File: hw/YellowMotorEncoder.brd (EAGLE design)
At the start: 35 x 22.2 mm, 20 parts, among them P1 M1

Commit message: FourProbes
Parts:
- removed C2: 10n/50V, rcl:C0402
- removed JP1: (no value), pinhead:1X06
- removed U$3: YELLOW_MOTOR, motor:YELLOW_MOTOR
- added C10: 20n/50V, rcl:C0402
- added C8, C9: 18p/50V, rcl:C0402
- added M1: MOTOR, motor:OT-FK-130PH
- added R6, R7: 47k, rcl:R0402
- added U$4, U$5: MH253ESO, hall_sensor:SOT23
- added U1: SN74LVC2G86DCTR, SN74LVC2G86DCTR:SOP65P400X130-8N
- C1: value 10n/50V -> 20n/50V
- R1, R2, R3, R4, R5: device rcl:R0603 -> rcl:R0402
- moved C3 29.9 mm to (2.00, 7.30)
- moved C5 23.5 mm to (8.85, 4.55), turned to 0 degrees
- moved C4 18.4 mm to (18.1, 7.40), turned to 270 degrees
- moved LED_B 17.8 mm to (18.4, 1.30), turned to 0 degrees
- moved P1 15.7 mm to (10.8, 1.90), turned to 180 degrees
- moved R3 13.6 mm to (18.4, 3.50), turned to 270 degrees
- moved LED_A 13.3 mm to (2.95, 1.30), turned to 0 degrees
- moved R2 13.3 mm to (2.95, 3.60), turned to 270 degrees
- moved LED_POWER 11.2 mm to (1.70, 1.30)
- moved U$1 10.9 mm to (11.8, 17.2), turned to 270 degrees
- moved R4 10.1 mm to (11.8, 14.9), turned to 180 degrees
- moved R5 9.28 mm to (5.00, 13.2), turned to 180 degrees
- moved R1 7.76 mm to (1.70, 3.60), turned to 270 degrees
- moved C6 6.42 mm to (15.4, 10.8), turned to 0 degrees
- moved C1 5.51 mm to (2.50, 13.0), turned to 270 degrees
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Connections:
- new net A0: C8.1, R6.1, U$4.2, U1.6
- new net A1: C9.1, R7.1, U$5.2, U1.5
- new net B0: C6.1, R4.1, U$1.2, U1.2
- new net B1: C7.1, R5.1, U$2.2, U1.1
- net A: now also U1.3; no longer C6.1, JP1.4, R4.1, U$1.2
- net B: now also U1.7; no longer C7.1, JP1.3, R5.1, U$2.2
- net GND: now also C10.2, C8.2, C9.2, U$4.3, U$5.3, U1.8; no longer C2.2, JP1.2
- net M+: now also M1.P$1; no longer JP1.6, U$3.P$2
- net M-: now also M1.P$2; no longer JP1.1, U$3.P$1
- net VCC: now also C10.1, R6.2, R7.2, U$4.1, U$5.1, U1.4; no longer C2.1, JP1.5
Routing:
- net A1: track 0.00 -> 27.1 mm, vias 0 -> 3
- net VCC: track 50.4 -> 76.3 mm, vias 3 -> 2
- net B1: track 0.00 -> 19.5 mm, vias 0 -> 2
- net A0: track 0.00 -> 17.8 mm, vias 0 -> 2
- net M-: track 3.63 -> 18.8 mm
- net B: track 25.8 -> 11.9 mm, vias 0 -> 1
- net M+: track 3.63 -> 17.2 mm
- net B0: track 0.00 -> 11.1 mm, vias 0 -> 2
- net A: track 27.0 -> 21.0 mm
- net LED_TOP1: track 3.94 -> 0.95 mm
- net LED_SIDE1: track 3.94 -> 1.05 mm
- net LED_POWER: track 1.93 -> 1.05 mm
- removed copper zone on layer 1, net M+
- removed copper zone on layer 16, net M+
- removed copper zone on layer 1, net M-
- removed copper zone on layer 16, net M-
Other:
- board size 35 x 22.2 mm -> 20 x 21 mm
- board text removed: "A"
- board text removed: "B"
- board text removed: "JLCJLCJLCJLC"
- board text removed: "M- GND B A VCC M+"
- board text removed: "RB0003-YellowMotorEncoder"
- board text removed: "YellowMotorEncoder"
- board text removed: "github::roboticsbrno/"
- board text removed: "v1.2 CC BY-SA 4.0"

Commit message: ochrany
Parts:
- added C2: 20n/50V, rcl_upravena:C0402
- added Q1: FDN360P, transistor-power:SUPER-SOT3
- added R8, R9: 200, rcl_upravena:R0402
- C1, C10, C6, C7, C8, C9: device rcl:C0402 -> rcl_upravena:C0402
- M1: value MOTOR -> YELLOW_MOTORV2; device motor:OT-FK-130PH -> motor:YELLOW_MOTOR_V2
- R1, R2, R3, R4, R5, R6, R7: device rcl:R0402 -> rcl_upravena:R0402
- moved LED_A 17.4 mm to (17.4, 11.0), turned to 180 degrees
- moved R2 15.5 mm to (17.7, 8.50), turned to 90 degrees
- moved R6 12.7 mm to (2.90, 10.3)
- moved U$4 12.4 mm to (2.93, 12.5)
- moved C7 12.0 mm to (16.4, 10.6), turned to 90 degrees
- moved C8 10.2 mm to (5.15, 10.8), turned to 90 degrees
- moved C4 9.98 mm to (16.9, 17.3), turned to 90 degrees
- moved C5 9.73 mm to (18.1, 1.70), turned to 90 degrees
- moved LED_B 9.70 mm to (18.5, 11.0), turned to 180 degrees
- moved C9 8.08 mm to (13.1, 4.70), turned to 270 degrees
- moved C10 5.28 mm to (14.6, 17.1), turned to 0 degrees
- moved R3 5.00 mm to (18.6, 8.50), turned to 90 degrees
- moved C1 3.06 mm to (2.75, 16.1), turned to 90 degrees
- moved C3 2.39 mm to (4.00, 8.60), turned to 0 degrees
- moved P1 0.90 mm to (9.85, 1.95)
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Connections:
- new net !A: R2.1, R8.1, U1.7
- new net !B: R3.1, R9.1, U1.3
- new net N$1: P1.2, Q1.3
- net A: now also R8.2; no longer R2.1, U1.3
- net A0: now also U1.2; no longer U1.6
- net A1: now also U1.1; no longer U1.5
- net B: now also R9.2; no longer R3.1, U1.7
- net B0: now also U1.6; no longer U1.2
- net B1: now also U1.5; no longer U1.1
- net GND: now also C2.2, Q1.1, U1.4; no longer U1.8
- net VCC: now also C2.1, Q1.2, U1.8; no longer P1.2, U1.4
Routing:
- net A: track 21.0 -> 2.79 mm
- net !A: track 0.00 -> 14.6 mm, vias 0 -> 2
- net !B: track 0.00 -> 12.2 mm, vias 0 -> 2
- net VCC: track 76.3 -> 66.3 mm, vias 2 -> 3
- net B: track 11.9 -> 2.36 mm, vias 1 -> 0
- net A1: track 27.1 -> 19.8 mm, vias 3 -> 2
- net B1: track 19.5 -> 25.6 mm
- net B0: track 11.1 -> 16.8 mm
- net M+: track 17.2 -> 21.3 mm
- net N$1: track 0.00 -> 3.53 mm
- net A0: track 17.8 -> 20.7 mm
- net M-: track 18.8 -> 20.0 mm
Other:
- outline, holes or cut-outs redrawn

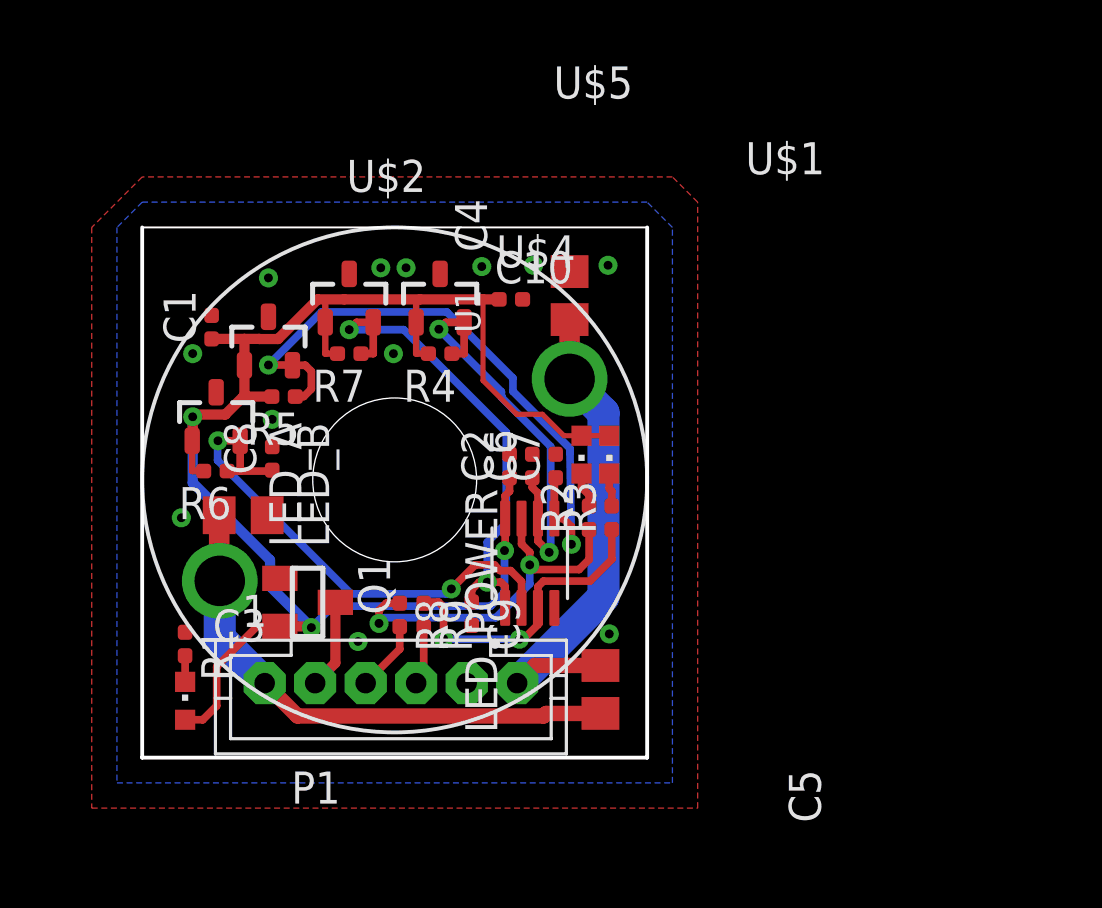
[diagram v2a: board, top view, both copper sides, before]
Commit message: YellowMotorEncoder_V2.0
New design with four sensors and xor to combine two signals to one.
Design is in KiCad.
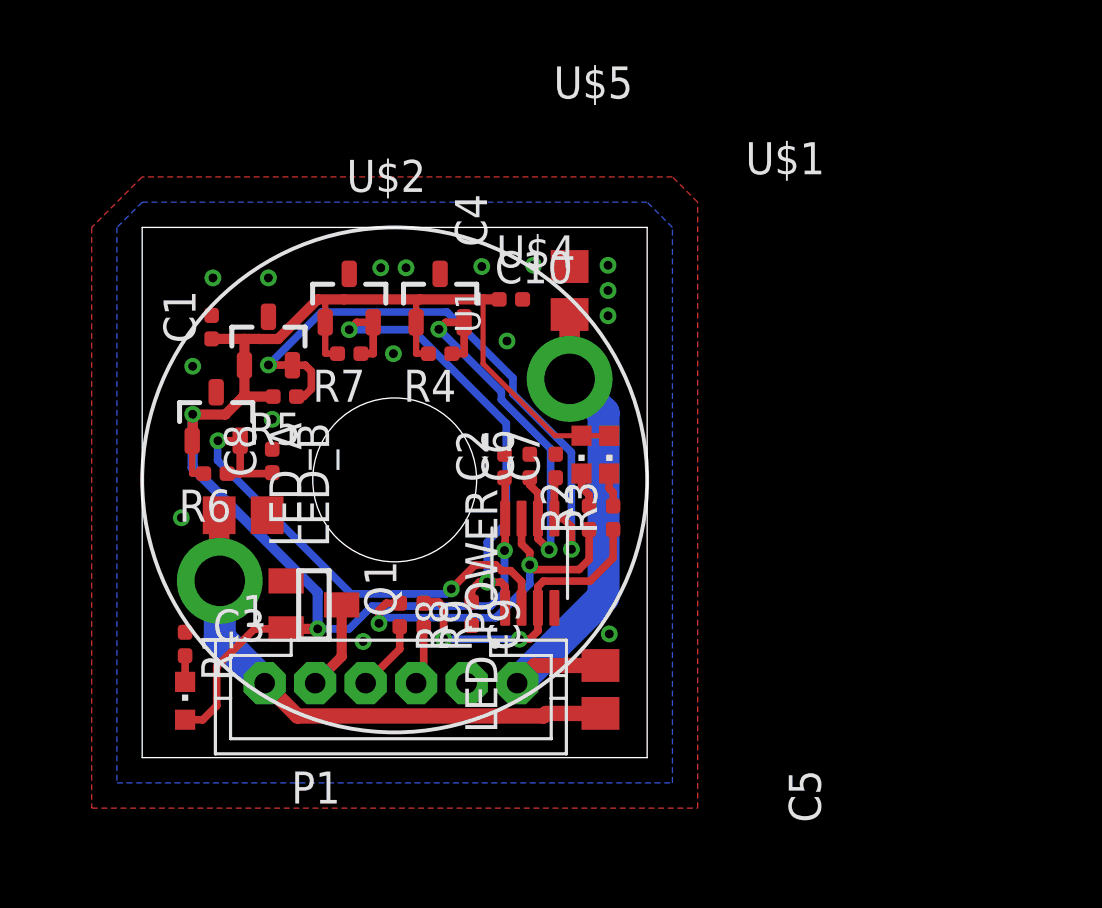
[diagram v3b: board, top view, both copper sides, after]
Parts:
- moved Q1 0.27 mm to (6.80, 5.05)
- moved C2 0.20 mm to (14.3, 10.6)
- moved C4 0.20 mm to (16.9, 17.5)
- moved C6 0.10 mm to (15.3, 10.6)
- moved C8 0.10 mm to (5.15, 10.8)
- moved R6 0.10 mm to (2.90, 10.2)
- moved R5 0.05 mm to (5.65, 13.3)
